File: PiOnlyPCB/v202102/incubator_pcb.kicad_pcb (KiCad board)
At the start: 2 copper layers, 85.1 x 55.9 mm, 34 parts, among them J1 Conn_01x04, J10 Conn_01x02, J11 Conn_01x02, J2 Conn_01x04, J3 Conn_01x04, J4 Conn_01x02, J5 Conn_01x02, J6 Conn_01x02, J7 Conn_01x02, J8 Conn_01x02, J9 Conn_01x02, Q1 Q_NMOS_GDS, Q2 Q_NMOS_GDS, Q3 Q_NMOS_GDS, Q4 Q_NMOS_GDS, U1 header_pi_zero_w

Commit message: Partial version with GPIO expander too.
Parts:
- removed D2, D3: LED, Diode_SMD:D_0805_2012Metric_Pad1.15x1.40mm_HandSolder
- removed J10, J11: Conn_01x02, TerminalBlock_Phoenix:TerminalBlock_Phoenix_MKDS-1,5-2_1x02_P5.00mm_Horizontal
- removed R10, R12, R4, R6: R_Small, Resistor_SMD:R_0805_2012Metric_Pad1.15x1.40mm_HandSolder
- added C1: C, Capacitor_SMD:C_0805_2012Metric_Pad1.18x1.45mm_HandSolder, B.Cu at (66.7, 109.9)
- added C2: C, Capacitor_SMD:C_0805_2012Metric_Pad1.18x1.45mm_HandSolder, B.Cu at (92.1, 109.2)
- added Q10: Q_NMOS_GDS, Package_TO_SOT_SMD:TO-252-2, F.Cu at (93.2, 92.4)
- added Q11: Q_NMOS_GDS, Package_TO_SOT_SMD:TO-252-2, F.Cu at (93.2, 110.8)
- added Q12: Dual_NMOSFET_BUK9K22_80E_Swapped, v202102_OpenPlant:LFPAK56D, B.Cu at (95.8, 85.1)
- added Q13: Q_NMOS_GDS, Package_TO_SOT_SMD:TO-252-2, F.Cu at (61.2, 92.4)
- added Q14: Q_NMOS_GDS, Package_TO_SOT_SMD:TO-252-2, F.Cu at (61.2, 110.8)
- added Q15: Dual_NMOSFET_BUK9K22_80E_Swapped, v202102_OpenPlant:LFPAK56D, B.Cu at (63.8, 85.1)
- added Q16: Q_NMOS_GDS, Package_TO_SOT_SMD:TO-252-2, F.Cu at (71.9, 92.4)
- added Q17: Q_NMOS_GDS, Package_TO_SOT_SMD:TO-252-2, F.Cu at (71.9, 110.8)
- added Q18: Dual_NMOSFET_BUK9K22_80E_Swapped, v202102_OpenPlant:LFPAK56D, B.Cu at (74.4, 85.1)
- added Q5: Q_NMOS_GDS, Package_TO_SOT_SMD:TO-252-2, F.Cu at (50.5, 110.8)
- added Q6: Dual_NMOSFET_BUK9K22_80E_Swapped, v202102_OpenPlant:LFPAK56D, B.Cu at (53.1, 85.1)
- added Q7: Q_NMOS_GDS, Package_TO_SOT_SMD:TO-252-2, F.Cu at (82.5, 92.4)
- added Q8: Q_NMOS_GDS, Package_TO_SOT_SMD:TO-252-2, F.Cu at (82.5, 110.8)
- added Q9: Dual_NMOSFET_BUK9K22_80E_Swapped, v202102_OpenPlant:LFPAK56D, B.Cu at (85.1, 85.1)
- added R17: R_Small, Resistor_SMD:R_0805_2012Metric_Pad1.20x1.40mm_HandSolder, F.Cu at (85.3, 100.4)
- added R19: R_Small, Resistor_SMD:R_0805_2012Metric_Pad1.20x1.40mm_HandSolder, F.Cu at (85.3, 119.3)
- added R20: R_Small, Resistor_SMD:R_0805_2012Metric_Pad1.20x1.40mm_HandSolder, F.Cu at (90.9, 100.4)
- added R21: R_Small, Resistor_SMD:R_0805_2012Metric_Pad1.20x1.40mm_HandSolder, F.Cu at (90.9, 119.3)
- added R23: R_Small, Resistor_SMD:R_0805_2012Metric_Pad1.20x1.40mm_HandSolder, F.Cu at (96.0, 100.4)
- added R25: R_Small, Resistor_SMD:R_0805_2012Metric_Pad1.20x1.40mm_HandSolder, F.Cu at (96.0, 119.3)
- added R26: R_Small, Resistor_SMD:R_0805_2012Metric_Pad1.20x1.40mm_HandSolder, F.Cu at (58.9, 100.4)
- added R27: R_Small, Resistor_SMD:R_0805_2012Metric_Pad1.20x1.40mm_HandSolder, F.Cu at (58.9, 119.3)
- added R29: R_Small, Resistor_SMD:R_0805_2012Metric_Pad1.20x1.40mm_HandSolder, F.Cu at (64.0, 100.4)
- added R31: R_Small, Resistor_SMD:R_0805_2012Metric_Pad1.20x1.40mm_HandSolder, F.Cu at (64.0, 119.3)
- added R32: R_Small, Resistor_SMD:R_0805_2012Metric_Pad1.20x1.40mm_HandSolder, F.Cu at (69.6, 100.4)
- added R33: R_Small, Resistor_SMD:R_0805_2012Metric_Pad1.20x1.40mm_HandSolder, F.Cu at (69.6, 119.3)
- added R35: R_Small, Resistor_SMD:R_0805_2012Metric_Pad1.20x1.40mm_HandSolder, F.Cu at (74.7, 100.4)
- added R37: R_Small, Resistor_SMD:R_0805_2012Metric_Pad1.20x1.40mm_HandSolder, F.Cu at (74.7, 119.3)
- added R38: R_Small, Resistor_SMD:R_0805_2012Metric_Pad1.20x1.40mm_HandSolder, B.Cu at (92.1, 120.0)
- added R39: R_Small, Resistor_SMD:R_0805_2012Metric_Pad1.20x1.40mm_HandSolder, B.Cu at (92.1, 114.3)
- added R40: R_Small, Resistor_SMD:R_0805_2012Metric_Pad1.20x1.40mm_HandSolder, B.Cu at (66.7, 120.0)
- added R41: R_Small, Resistor_SMD:R_0805_2012Metric_Pad1.20x1.40mm_HandSolder, B.Cu at (66.7, 114.9)
- added R42: R_Small, Resistor_SMD:R_0805_2012Metric_Pad1.20x1.40mm_HandSolder, B.Cu at (94.0, 120.0)
- added R43: R_Small, Resistor_SMD:R_0805_2012Metric_Pad1.20x1.40mm_HandSolder, B.Cu at (94.0, 114.3)
- added R44: R_Small, Resistor_SMD:R_0805_2012Metric_Pad1.20x1.40mm_HandSolder, B.Cu at (68.6, 120.0)
- added R45: R_Small, Resistor_SMD:R_0805_2012Metric_Pad1.20x1.40mm_HandSolder, B.Cu at (68.6, 114.9)
- added R46: R_Small, Resistor_SMD:R_0805_2012Metric_Pad1.20x1.40mm_HandSolder, B.Cu at (95.9, 120.0)
- added R47: R_Small, Resistor_SMD:R_0805_2012Metric_Pad1.20x1.40mm_HandSolder, B.Cu at (95.9, 114.3)
- added R48: R_Small, Resistor_SMD:R_0805_2012Metric_Pad1.20x1.40mm_HandSolder, B.Cu at (70.5, 120.0)
- added R49: R_Small, Resistor_SMD:R_0805_2012Metric_Pad1.20x1.40mm_HandSolder, B.Cu at (70.5, 114.9)
- added R50: R_Small, Resistor_SMD:R_0805_2012Metric_Pad1.20x1.40mm_HandSolder, B.Cu at (61.6, 103.9)
- added R51: R_Small, Resistor_SMD:R_0805_2012Metric_Pad1.20x1.40mm_HandSolder, B.Cu at (63.5, 103.9)
- added R52: R_Small, Resistor_SMD:R_0805_2012Metric_Pad1.20x1.40mm_HandSolder, B.Cu at (87.0, 103.8)
- added R53: R_Small, Resistor_SMD:R_0805_2012Metric_Pad1.20x1.40mm_HandSolder, B.Cu at (88.9, 103.8)
- added R54: R_Small, Resistor_SMD:R_0805_2012Metric_Pad1.20x1.40mm_HandSolder, B.Cu at (85.1, 103.8)
- added R55: R_Small, Resistor_SMD:R_0805_2012Metric_Pad1.20x1.40mm_HandSolder, B.Cu at (59.7, 103.9)
- added U2: PCF8574, Package_SO:SOIC-16W_7.5x10.3mm_P1.27mm, B.Cu at (85.1, 113.0)
- added U3: PCF8574, Package_SO:SOIC-16W_7.5x10.3mm_P1.27mm, B.Cu at (59.7, 113.7)
- D1, U1: moved to F.Cu
- J1: value Conn_01x04 -> Conn_01x05; footprint Connector_PinHeader_2.54mm:PinHeader_1x04_P2.54mm_Vertical -> Connector_PinHeader_2.54mm:PinHeader_1x05_P2.54mm_Vertical
- J2: value Conn_01x04 -> Conn_01x12_Female; footprint Connector_PinHeader_2.54mm:PinHeader_1x04_P2.54mm_Vertical -> v202102_OpenPlant:PWRCON_3M81-12
- J3: value Conn_01x04 -> Conn_01x05_Female; footprint Connector_PinHeader_2.54mm:PinHeader_1x04_P2.54mm_Vertical -> v202102_OpenPlant:PWRCON_3M81-5
- J4, J5: value Conn_01x02 -> Conn_01x04; footprint TerminalBlock_Phoenix:TerminalBlock_Phoenix_MKDS-1,5-2_1x02_P5.00mm_Horizontal -> Connector_JST:JST_SH_BM04B-SRSS-TB_1x04-1MP_P1.00mm_Vertical
- J6, J7: value Conn_01x02 -> Conn_01x04; footprint TerminalBlock_Phoenix:TerminalBlock_Phoenix_MKDS-1,5-2_1x02_P5.00mm_Horizontal -> Connector_PinHeader_2.54mm:PinHeader_1x04_P2.54mm_Vertical
- J8, J9: value Conn_01x02 -> Conn_01x08; footprint TerminalBlock_Phoenix:TerminalBlock_Phoenix_MKDS-1,5-2_1x02_P5.00mm_Horizontal -> Connector_PinHeader_2.54mm:PinHeader_1x08_P2.54mm_Vertical
- Q1, Q2, Q4: footprint Package_TO_SOT_THT:TO-220-3_Vertical -> Package_TO_SOT_SMD:TO-252-2
- Q3: value Q_NMOS_GDS -> Dual_NMOSFET_BUK9K22_80E_Swapped; footprint Package_TO_SOT_THT:TO-220-3_Vertical -> v202102_OpenPlant:LFPAK56D; moved to B.Cu
- R1, R2, R3: footprint Resistor_SMD:R_0805_2012Metric_Pad1.15x1.40mm_HandSolder -> Resistor_SMD:R_0805_2012Metric_Pad1.20x1.40mm_HandSolder; moved to F.Cu
- R11, R13, R14, R15, R5, R7, R8, R9: footprint Resistor_SMD:R_0805_2012Metric_Pad1.15x1.40mm_HandSolder -> Resistor_SMD:R_0805_2012Metric_Pad1.20x1.40mm_HandSolder
- moved R1 62.1 mm to (7.62, 119.7), turned to 90 degrees
- moved J6 60.5 mm to (15.2, 95.6), turned to 90 degrees
- moved J7 57.1 mm to (15.2, 107.6), turned to 90 degrees
- moved D1 52.0 mm to (7.62, 115.3), turned to 90 degrees
- moved Q4 51.1 mm to (50.5, 92.4), turned to 90 degrees
- moved J8 48.2 mm to (64.8, 124.5), turned to 270 degrees
- moved U1 47.6 mm to (30.5, 76.8)
- moved R11 46.8 mm to (53.3, 100.4), turned to 90 degrees
- moved J5 46.2 mm to (8.26, 106.0), turned to 90 degrees
- moved Q3 41.4 mm to (42.4, 85.1), turned to 90 degrees
- moved J1 41.4 mm to (15.2, 83.2), turned to 90 degrees
- moved J4 41.2 mm to (8.26, 94.0), turned to 90 degrees
- moved J2 39.6 mm to (68.6, 69.8)
- moved R13 34.3 mm to (53.3, 119.3), turned to 90 degrees
- moved R3 33.3 mm to (37.6, 119.3), turned to 270 degrees
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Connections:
- D1 pad 2: Net-(D1-Pad2) -> VCC3V3
- J1 pad 2: GND -> VCC3V3
- J1 pad 3: GPIO2_I2C1_SCL -> GND
- J1 pad 4: GPIO2_I2C1_SDA -> VCC5V
- J2 pad 1: VCC3V3 -> /OUT1
- J2 pad 2: GND -> /OUT2
- J2 pad 3: GPIO2_I2C1_SCL -> /OUT3
- J2 pad 4: GPIO2_I2C1_SDA -> /OUT4
- J3 pad 1: VCC3V3 -> GND
- J3 pad 3: GPIO2_I2C1_SCL -> GND
- J3 pad 4: GPIO2_I2C1_SDA -> GND
- J4 pad 1: Net-(J4-Pad1) -> GND
- J4 pad 2: Net-(J4-Pad1) -> VCC3V3
- J5 pad 2: GND -> VCC3V3
- J6 pad 2: GND -> VCC3V3
- J7 pad 1: Net-(J7-Pad1) -> GND
- J7 pad 2: Net-(J7-Pad1) -> VCC3V3
- J8 pad 2: Net-(J8-Pad1) -> Net-(J8-Pad2)
- J9 pad 1: GND -> Net-(J9-Pad1)
- J9 pad 2: GND -> Net-(J9-Pad2)
- Q1 pad 2: Net-(J4-Pad1) -> /OUT1
- Q2 pad 2: Net-(J7-Pad1) -> /OUT2
- Q3 pad 1: Net-(Q3-Pad1) -> GND
- Q3 pad 2: Net-(J8-Pad1) -> Net-(Q2-Pad1)
- Q4 pad 2: Net-(J10-Pad1) -> /OUT3
- R1 pad 2: Net-(D3-Pad1) -> Net-(D1-Pad1)
- R11 pad 2: GPIO23 -> GND
- R13 pad 1: Net-(Q3-Pad1) -> Net-(Q5-Pad1)
- R14 pad 1: VCC3V3 -> Net-(Q7-Pad1)
- R14 pad 2: Net-(Q4-Pad1) -> /IN9
- R15 pad 1: Net-(Q4-Pad1) -> Net-(Q8-Pad1)
- R15 pad 2: GND -> /IN10
- R2 pad 1: GND -> Net-(Q1-Pad1)
- R2 pad 2: Net-(D1-Pad1) -> /IN1
- R3 pad 1: GND -> Net-(Q2-Pad1)
- R3 pad 2: Net-(D2-Pad1) -> /IN2
- R5 pad 1: Net-(Q2-Pad1) -> Net-(Q1-Pad1)
- R5 pad 2: GPIO13_PWM1 -> GND
- R7 pad 1: Net-(Q1-Pad1) -> Net-(Q2-Pad1)
- R8 pad 1: VCC3V3 -> Net-(Q4-Pad1)
- R8 pad 2: Net-(Q2-Pad1) -> /IN3
- R9 pad 1: Net-(Q2-Pad1) -> Net-(Q5-Pad1)
- R9 pad 2: GND -> /IN4
- U1 pad 15: GPIO22 -> /IN3
- U1 pad 16: GPIO23 -> /IN4
- U1 pad 18: Net-(D1-Pad2) -> /IN5
- U1 pad 19: (no net) -> /IN6
- U1 pad 21: (no net) -> /IN7
- U1 pad 22: (no net) -> /IN8
- U1 pad 23: (no net) -> /IN9
- U1 pad 24: Net-(D2-Pad2) -> /IN10
- U1 pad 26: (no net) -> /IN11
- U1 pad 27: (no net) -> /IN12
- U1 pad 32: GPIO12_PWM0 -> /IN1
- U1 pad 33: GPIO13_PWM1 -> /IN2
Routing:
- net GPIO23: track 71.5 -> 0.00 mm, vias 1 -> 0
- net /IN11: track 0.00 -> 70.2 mm, vias 0 -> 1
- net /IN12: track 0.00 -> 68.7 mm, vias 0 -> 1
- net /IN10: track 0.00 -> 61.3 mm, vias 0 -> 1
- net /IN8: track 0.00 -> 58.0 mm, vias 0 -> 1
- net GPIO22: track 57.9 -> 0.00 mm, vias 1 -> 0
- net /IN9: track 0.00 -> 55.5 mm, vias 0 -> 1
- net GND: track 294.9 -> 349.1 mm, vias 3 -> 51
- net /IN4: track 0.00 -> 53.3 mm, vias 0 -> 2
- net /IN6: track 0.00 -> 50.3 mm, vias 0 -> 2
- net /OUT12: track 0.00 -> 49.8 mm
- net /OUT2: track 0.00 -> 49.4 mm
- net /OUT10: track 0.00 -> 46.6 mm
- net /OUT4: track 0.00 -> 44.9 mm
- net /IN7: track 0.00 -> 44.9 mm, vias 0 -> 1
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- added copper zone on In1.Cu, net GND
- added copper zone on In2.Cu, net VCC3V3
- removed copper zone on B.Cu, net GND
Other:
- board size 85.1 x 55.9 mm -> 97.2 x 55.9 mm
- copper layers 2 -> 4
- net class HighPower added: clearance 0.45, trace_width 2.5, via_dia 0.8, via_drill 0.4
- board text removed: "NY Open Plant Incubator v2019-09-21"

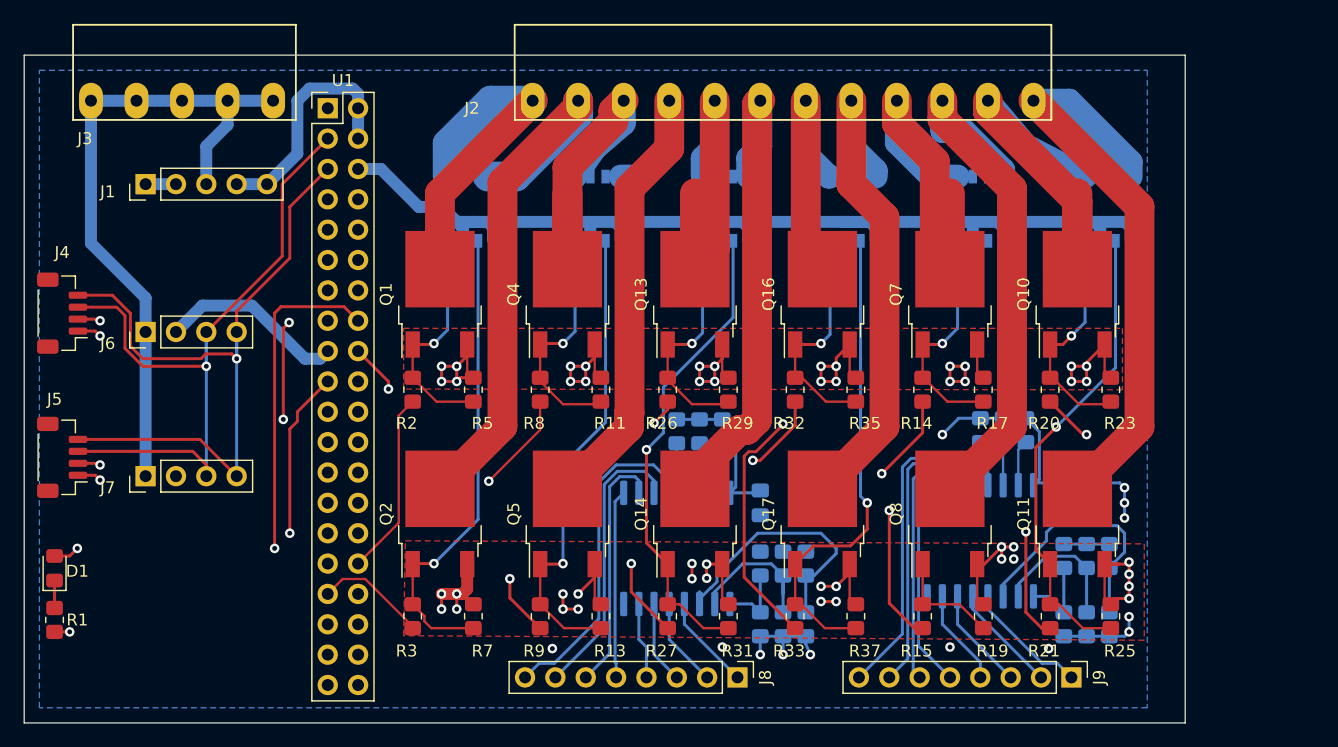
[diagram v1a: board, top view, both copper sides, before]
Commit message: PiOnlyPCB 202102: Routed again without I2C expanders, before IN* nets routed.
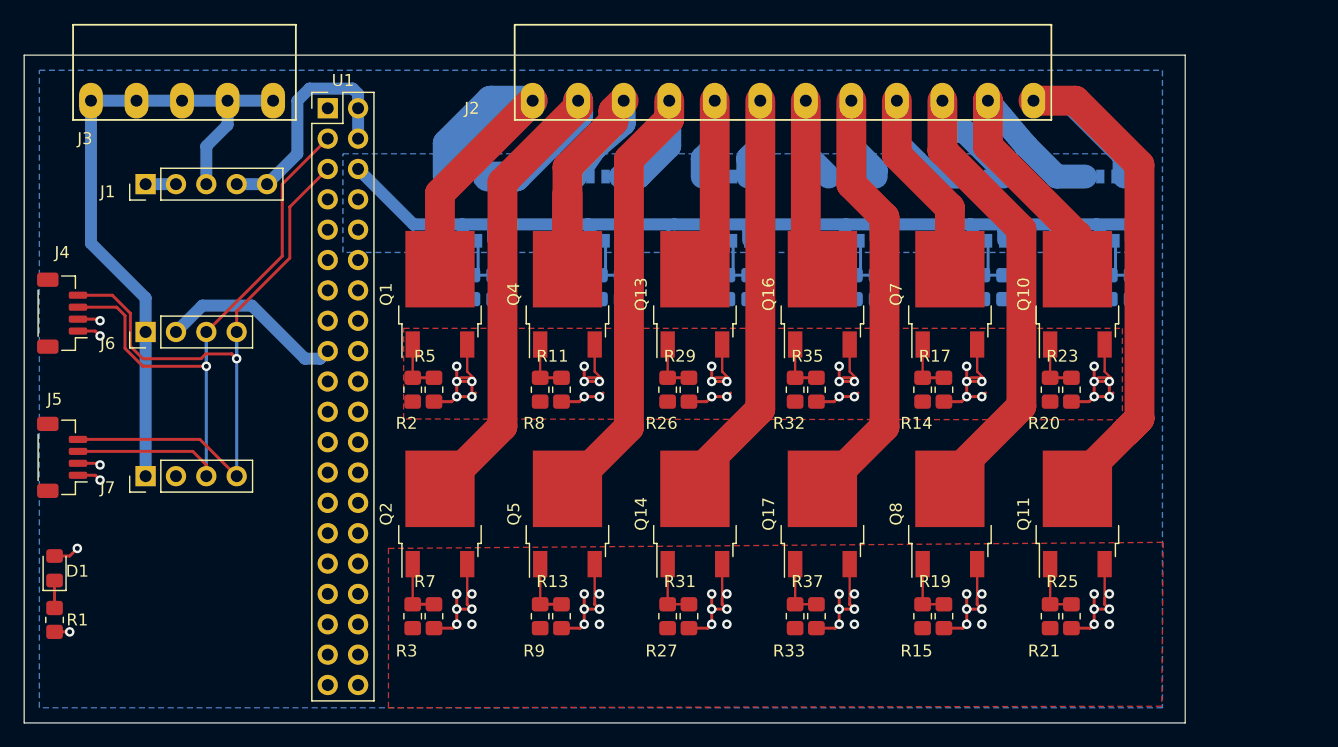
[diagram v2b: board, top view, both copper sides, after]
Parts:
- removed C1, C2: C, Capacitor_SMD:C_0805_2012Metric_Pad1.18x1.45mm_HandSolder
- removed J8, J9: Conn_01x08, Connector_PinHeader_2.54mm:PinHeader_1x08_P2.54mm_Vertical
- removed R50, R51, R52, R53, R54, R55: R_Small, Resistor_SMD:R_0805_2012Metric_Pad1.20x1.40mm_HandSolder
- removed U2, U3: PCF8574, Package_SO:SOIC-16W_7.5x10.3mm_P1.27mm
- added R10: R_Small, Resistor_SMD:R_0805_2012Metric_Pad1.20x1.40mm_HandSolder, B.Cu at (40.6, 91.8)
- added R12: R_Small, Resistor_SMD:R_0805_2012Metric_Pad1.20x1.40mm_HandSolder, B.Cu at (44.5, 91.8)
- added R16: R_Small, Resistor_SMD:R_0805_2012Metric_Pad1.20x1.40mm_HandSolder, B.Cu at (53.2, 91.8)
- added R18: R_Small, Resistor_SMD:R_0805_2012Metric_Pad1.20x1.40mm_HandSolder, B.Cu at (49.4, 91.8)
- added R22: R_Small, Resistor_SMD:R_0805_2012Metric_Pad1.20x1.40mm_HandSolder, B.Cu at (51.3, 91.8)
- added R24: R_Small, Resistor_SMD:R_0805_2012Metric_Pad1.20x1.40mm_HandSolder, B.Cu at (55.1, 91.8)
- added R28: R_Small, Resistor_SMD:R_0805_2012Metric_Pad1.20x1.40mm_HandSolder, B.Cu at (85.2, 91.8)
- added R30: R_Small, Resistor_SMD:R_0805_2012Metric_Pad1.20x1.40mm_HandSolder, B.Cu at (81.4, 91.8)
- added R34: R_Small, Resistor_SMD:R_0805_2012Metric_Pad1.20x1.40mm_HandSolder, B.Cu at (83.3, 91.8)
- added R36: R_Small, Resistor_SMD:R_0805_2012Metric_Pad1.20x1.40mm_HandSolder, B.Cu at (87.1, 91.8)
- added R4: R_Small, Resistor_SMD:R_0805_2012Metric_Pad1.20x1.40mm_HandSolder, B.Cu at (42.5, 91.8)
- added R6: R_Small, Resistor_SMD:R_0805_2012Metric_Pad1.20x1.40mm_HandSolder, B.Cu at (38.7, 91.8)
- moved R42 41.3 mm to (63.9, 91.8)
- moved R43 40.7 mm to (60.1, 91.8)
- moved R40 39.3 mm to (94.0, 91.8)
- moved R41 38.8 mm to (97.8, 91.8)
- moved R46 35.4 mm to (74.5, 91.8)
- moved R47 33.7 mm to (70.7, 91.8)
- moved R44 29.0 mm to (62.0, 91.8)
- moved R38 28.5 mm to (95.9, 91.8)
- moved R48 28.3 mm to (72.6, 91.8)
- moved R49 23.9 mm to (76.5, 91.8)
- moved R45 23.3 mm to (65.8, 91.8)
- moved R39 22.5 mm to (92.1, 91.8)
- moved R11 3.30 mm to (50.0, 100.4), turned to 270 degrees
- moved R13 3.30 mm to (50.0, 119.3), turned to 270 degrees
- moved R17 3.30 mm to (82.0, 100.4), turned to 270 degrees
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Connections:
- Q12 pad 2: Net-(Q11-Pad1) -> Net-(Q12-Pad2)
- Q12 pad 4: Net-(Q10-Pad1) -> Net-(Q12-Pad4)
- Q15 pad 2: Net-(Q14-Pad1) -> Net-(Q15-Pad2)
- Q15 pad 4: Net-(Q13-Pad1) -> Net-(Q15-Pad4)
- Q18 pad 2: Net-(Q17-Pad1) -> Net-(Q18-Pad2)
- Q18 pad 4: Net-(Q16-Pad1) -> Net-(Q18-Pad4)
- Q3 pad 2: Net-(Q2-Pad1) -> Net-(Q3-Pad2)
- Q3 pad 4: Net-(Q1-Pad1) -> Net-(Q3-Pad4)
- Q6 pad 2: Net-(Q5-Pad1) -> Net-(Q6-Pad2)
- Q6 pad 4: Net-(Q4-Pad1) -> Net-(Q6-Pad4)
- Q9 pad 2: Net-(Q8-Pad1) -> Net-(Q9-Pad2)
- Q9 pad 4: Net-(Q7-Pad1) -> Net-(Q9-Pad4)
- R38 pad 1: Net-(R38-Pad1) -> Net-(Q12-Pad2)
- R38 pad 2: VCC3V3 -> /IN12
- R39 pad 1: GND -> Net-(Q12-Pad4)
- R39 pad 2: Net-(R38-Pad1) -> GND
- R40 pad 1: Net-(R40-Pad1) -> Net-(Q12-Pad4)
- R40 pad 2: VCC3V3 -> /IN11
- R41 pad 1: GND -> Net-(Q12-Pad2)
- R41 pad 2: Net-(R40-Pad1) -> GND
- R42 pad 1: Net-(R42-Pad1) -> Net-(Q15-Pad2)
- R42 pad 2: VCC3V3 -> /IN6
- R43 pad 1: GND -> Net-(Q15-Pad4)
- R43 pad 2: Net-(R42-Pad1) -> GND
- R44 pad 1: Net-(R44-Pad1) -> Net-(Q15-Pad4)
- R44 pad 2: VCC3V3 -> /IN5
- R45 pad 1: GND -> Net-(Q15-Pad2)
- R45 pad 2: Net-(R44-Pad1) -> GND
- R46 pad 1: Net-(R46-Pad1) -> Net-(Q18-Pad2)
- R46 pad 2: VCC3V3 -> /IN8
- R47 pad 1: GND -> Net-(Q18-Pad4)
- R47 pad 2: Net-(R46-Pad1) -> GND
- R48 pad 1: Net-(R48-Pad1) -> Net-(Q18-Pad4)
- R48 pad 2: VCC3V3 -> /IN7
- R49 pad 1: GND -> Net-(Q18-Pad2)
- R49 pad 2: Net-(R48-Pad1) -> GND
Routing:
- net GND: track 349.1 -> 588.9 mm, vias 51 -> 69
- net VCC3V3: track 264.0 -> 85.2 mm, vias 16 -> 3
- net /IN11: track 70.2 -> 0.00 mm, vias 1 -> 0
- net /IN12: track 68.7 -> 0.00 mm, vias 1 -> 0
- net /IN10: track 61.3 -> 0.00 mm, vias 1 -> 0
- net /IN8: track 58.0 -> 0.00 mm, vias 1 -> 0
- net /IN9: track 55.5 -> 0.00 mm, vias 1 -> 0
- net /IN4: track 53.3 -> 0.00 mm, vias 2 -> 0
- net /IN6: track 50.3 -> 0.00 mm, vias 2 -> 0
- net /IN7: track 44.9 -> 0.00 mm, vias 1 -> 0
- net /IN3: track 41.7 -> 0.00 mm, vias 3 -> 0
- net Net-(Q17-Pad1): track 40.9 -> 5.15 mm, vias 1 -> 0
- net Net-(Q14-Pad1): track 40.1 -> 5.15 mm, vias 1 -> 0
- net Net-(Q2-Pad1): track 39.9 -> 5.15 mm, vias 1 -> 0
- net Net-(Q5-Pad1): track 39.7 -> 5.15 mm, vias 1 -> 0
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- added copper zone on B.Cu, net GND

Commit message: Routed signals
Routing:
- net /IN12: track 0.00 -> 93.2 mm, vias 0 -> 2
- net /IN11: track 0.00 -> 88.9 mm, vias 0 -> 2
- net /IN9: track 0.00 -> 81.6 mm, vias 0 -> 2
- net /IN10: track 0.00 -> 80.9 mm, vias 0 -> 2
- net /IN8: track 0.00 -> 68.3 mm, vias 0 -> 2
- net /IN6: track 0.00 -> 62.2 mm, vias 0 -> 1
- net /IN7: track 0.00 -> 59.4 mm, vias 0 -> 2
- net /IN4: track 0.00 -> 49.6 mm, vias 0 -> 2
- net /IN2: track 0.00 -> 43.2 mm, vias 0 -> 2
- net /IN5: track 0.00 -> 43.0 mm, vias 0 -> 1
- net /IN1: track 0.00 -> 43.0 mm, vias 0 -> 2
- net /IN3: track 0.00 -> 38.6 mm, vias 0 -> 1
- net GND: track 588.9 -> 610.5 mm
- net /OUT10: track 47.5 -> 46.6 mm
- removed copper zone on B.Cu, net VCC3V3

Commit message: PCB Ready to order. Passed DRC.
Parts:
- added J8: Conn_02x03_Odd_Even, Connector_PinHeader_2.54mm:PinHeader_2x03_P2.54mm_Vertical, F.Cu at (15.7, 121.2)
- moved R13 0.38 mm to (50.4, 119.4)
- moved R19 0.38 mm to (82.4, 119.4)
- moved R25 0.38 mm to (93.1, 119.4)
- moved R31 0.38 mm to (61.1, 119.4)
- moved R37 0.38 mm to (71.8, 119.4)
- moved R7 0.38 mm to (39.8, 119.4)
- moved R11 0.26 mm to (50.3, 100.4)
- moved R17 0.26 mm to (82.3, 100.4)
- moved R23 0.26 mm to (93.0, 100.4)
- moved R35 0.26 mm to (71.6, 100.4)
- moved R5 0.26 mm to (39.6, 100.4)
- moved R29 0.26 mm to (61.0, 100.4)
- moved R14 0.06 mm to (80.3, 100.4)
- moved R2 0.06 mm to (37.6, 100.4)
- moved R20 0.06 mm to (90.9, 100.4)
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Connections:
- U1 pad 11: (no net) -> ADL1
- U1 pad 12: (no net) -> ADL2
- U1 pad 13: (no net) -> ADL3
- U1 pad 36: (no net) -> ADL4
- U1 pad 37: (no net) -> ADL5
- U1 pad 38: (no net) -> ADL6
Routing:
- net ADL1: track 0.00 -> 42.5 mm
- net ADL2: track 0.00 -> 40.1 mm
- net ADL3: track 0.00 -> 38.4 mm
- net ADL4: track 0.00 -> 16.3 mm
- net ADL6: track 0.00 -> 13.8 mm
- net ADL5: track 0.00 -> 10.2 mm
- net GND: track 610.5 -> 617.9 mm
- net /IN5: track 43.0 -> 40.0 mm
- net /OUT2: track 49.6 -> 51.2 mm
- net /OUT3: track 31.6 -> 32.9 mm
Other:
- board text added: "3V3"
- board text added: "5V"
- board text added: "GND"
- board text added: "GP16"
- board text added: "GP17"
- board text added: "GP18"
- board text added: "GP20"
- board text added: "GP26"
- board text added: "GP27"
- board text added: "Open Plant Incubator v202102"
- board text added: "SCL"
- board text added: "SDA"

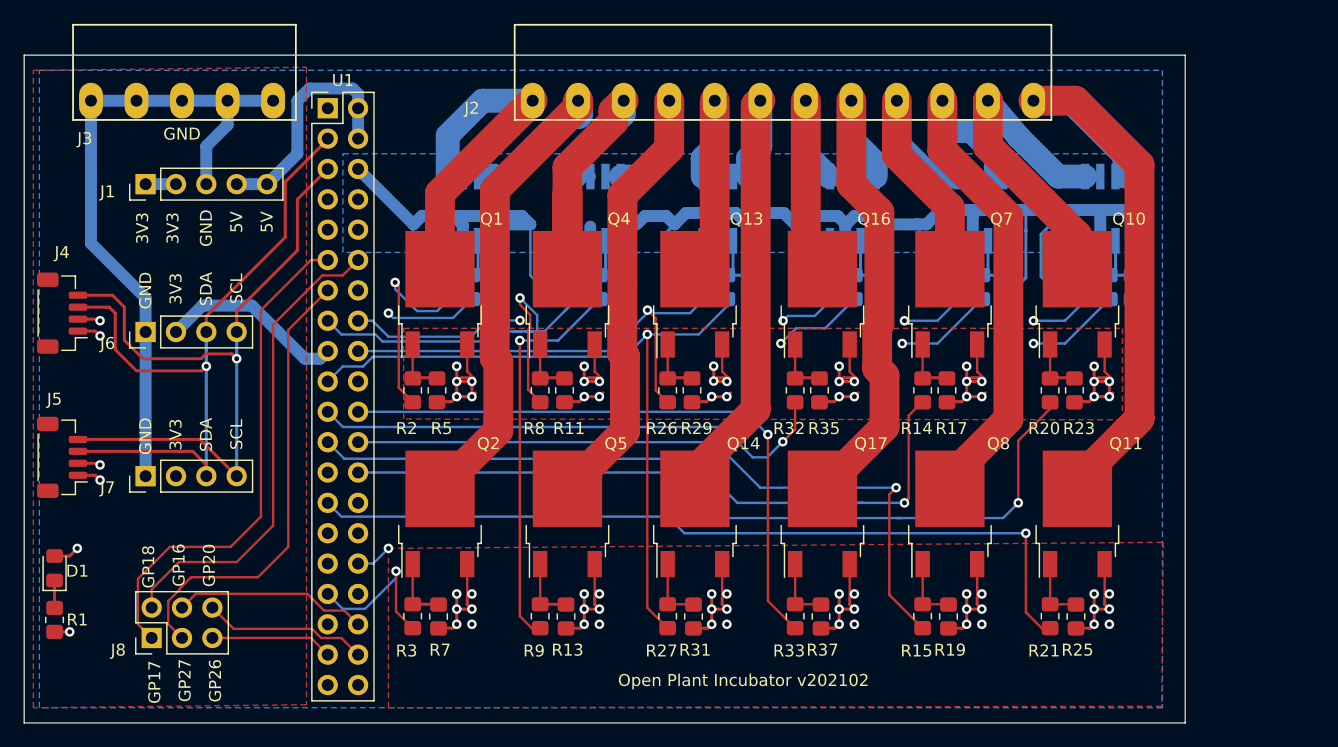
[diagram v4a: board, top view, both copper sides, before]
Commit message: v202102 sent out to fab.
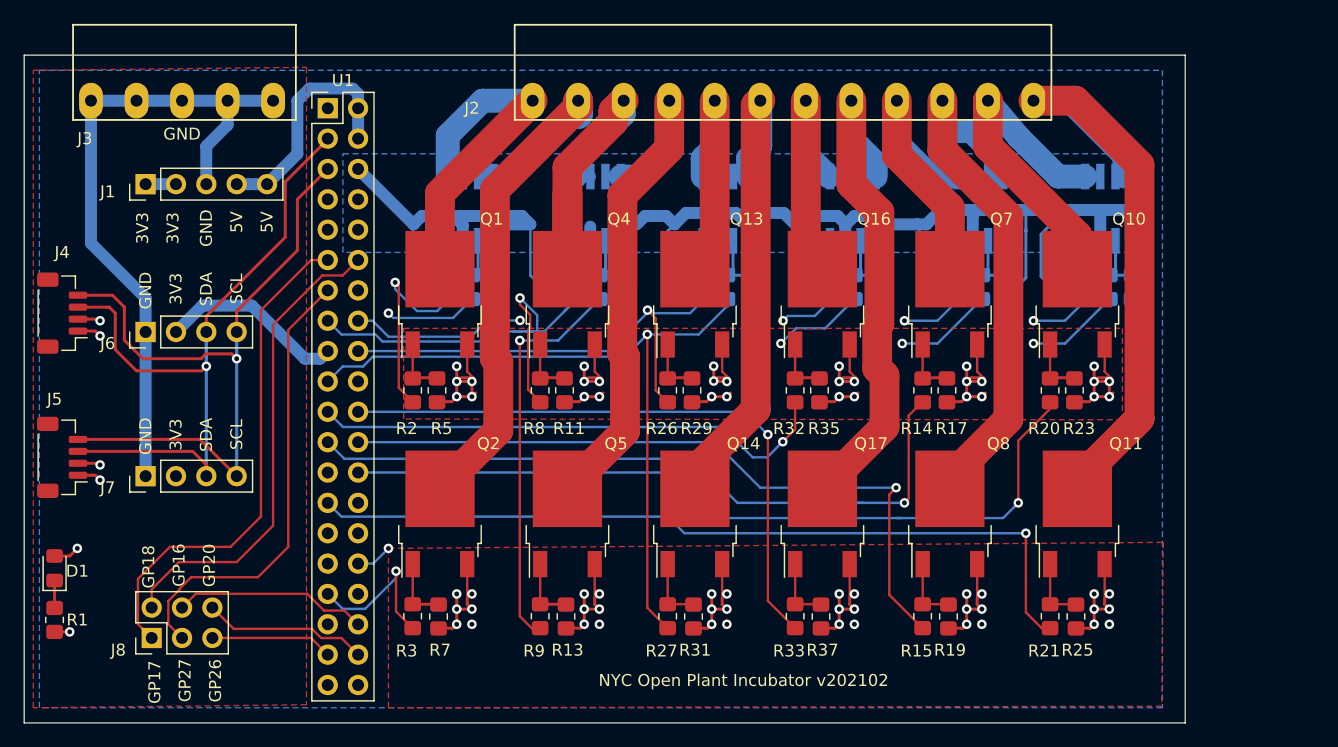
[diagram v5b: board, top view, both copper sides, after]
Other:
- board text added: "NYC Open Plant Incubator v202102"
- board text removed: "Open Plant Incubator v202102"
